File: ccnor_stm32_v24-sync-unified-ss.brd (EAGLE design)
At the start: 74.6 x 100 mm, 148 parts, among them J1 M02PT, J2 M021P25, J3 M02XH, J4 M021P25, Q1 2N7002P, Q2 WSP4406, Q3 WSP4406, Q4 NCE3018AS, Q5 IRLB8314PBF, Q6 2302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

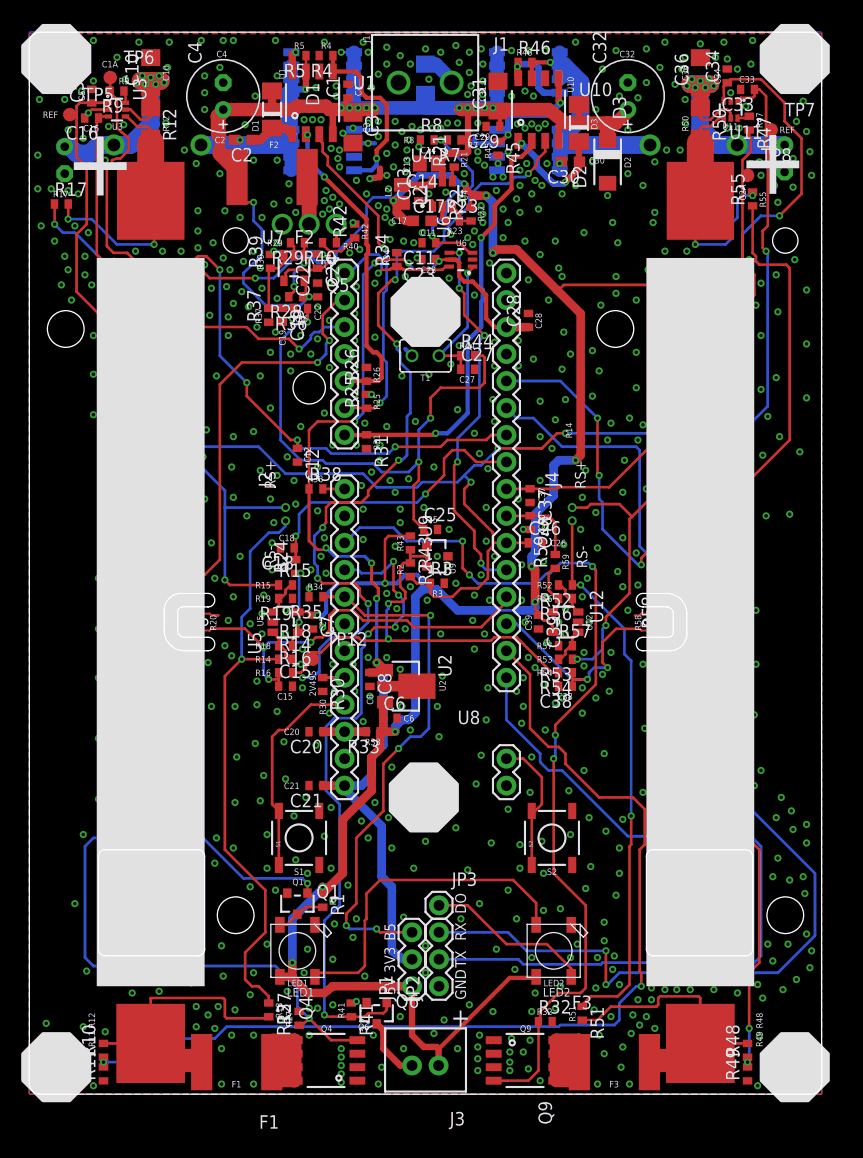
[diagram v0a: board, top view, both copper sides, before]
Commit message: Added TL431 through-hole, fixed DRC errors
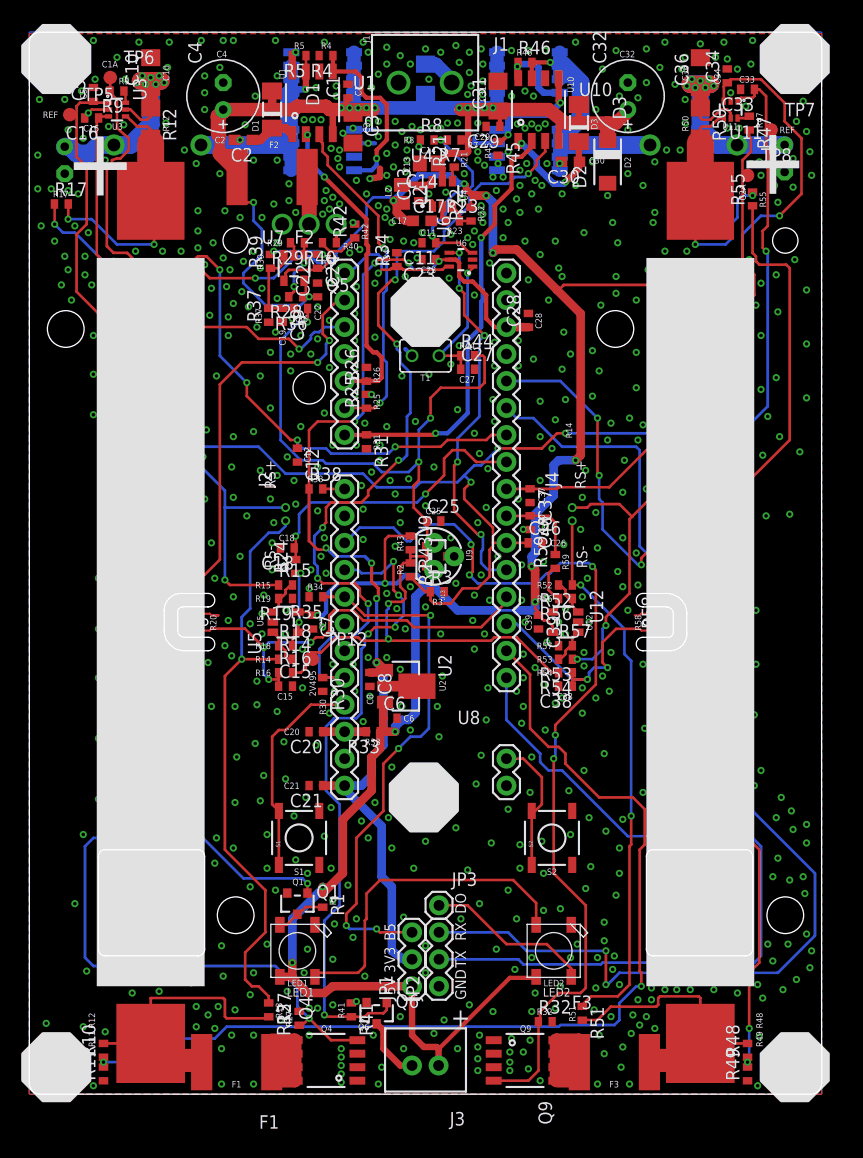
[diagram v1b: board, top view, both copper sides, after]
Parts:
- added U13: TL431TO92, custom:TO-92
- moved C25 0.85 mm to (38.1, 54.0)
- moved R3 0.79 mm to (38.4, 47.3)
- moved C5 0.22 mm to (6.03, 94.1)
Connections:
- net 2V495: now also U13.1, U13.3
- net GND: now also U13.2
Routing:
- net C2ON: track 86.9 -> 88.9 mm
- net C2COFF: track 81.0 -> 79.2 mm, vias 8 -> 7
- net 2V495: track 97.1 -> 98.7 mm
- net 7V4: track 147.3 -> 145.9 mm, vias 13 -> 12
- net ISNS_REF: track 162.3 -> 163.3 mm
- net AUX_SNS: track 36.1 -> 36.6 mm
- net GND: vias 805 -> 802
